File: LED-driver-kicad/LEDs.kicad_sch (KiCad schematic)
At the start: 54 parts, among them Q8 Q_NMOS_GDS, U6 MIC3205YML-TR, U7 MIC3205YML-TR, U8 MIC3205YML-TR

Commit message: initial PCB layout
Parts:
- removed D10: BAT42, Diode_THT:D_DO-35_SOD27_P7.62mm_Horizontal, symbol Diode:BAT42
- added D10: SD103AWS, Diode_SMD:D_SOD-323_HandSoldering, symbol Device:D_Schottky_Small
- D17, D24: value BAT42 -> SD103AWS; footprint Diode_THT:D_DO-35_SOD27_P7.62mm_Horizontal -> Diode_SMD:D_SOD-323_HandSoldering; symbol Diode:BAT42 -> Device:D_Schottky_Small
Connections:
- net +28V: now also D10.1 (K)
- net at L4.2, Q8.2 (D): now also D10.2 (A)
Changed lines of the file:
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@@
     (stroke (width 0) (type default))
   )
-  (wire (pts (xy 174.625 63.5) (xy 202.565 63.5))
+  (wire (pts (xy 174.625 63.5) (xy 203.835 63.5))
     (stroke (width 0) (type default))
   )
@@
     (stroke (width 0) (type default))
   )
-  (wire (pts (xy 83.185 114.3) (xy 117.475 114.3))
+  (wire (pts (xy 81.915 114.3) (xy 117.475 114.3))
     (stroke (width 0) (type default))
   )
@@
     (stroke (width 0) (type default))
   )
-  (wire (pts (xy 47.625 31.75) (xy 75.565 31.75))
+  (wire (pts (xy 47.625 31.75) (xy 76.2 31.75))
     (stroke (width 0) (type default))
   )
@@
     (stroke (width 0) (type default))
   )
-  (wire (pts (xy 47.625 114.3) (xy 75.565 114.3))
-    (stroke (width 0) (type default))
-  )
   (wire (pts (xy 186.69 82.55) (xy 186.69 93.98))
     (stroke (width 0) (type default))
@@
     (stroke (width 0) (type default))
   )
-  (wire (pts (xy 210.185 63.5) (xy 244.475 63.5))
+  (wire (pts (xy 208.915 63.5) (xy 244.475 63.5))
     (stroke (width 0) (type default))
   )
@@
     (stroke (width 0) (type default))
   )
-  (wire (pts (xy 83.185 31.75) (xy 117.475 31.75))
-    (stroke (width 0) (type default))
-  )
   (wire (pts (xy 80.645 133.35) (xy 102.235 133.35))
     (stroke (width 0) (type default))
   )
+  (wire (pts (xy 81.28 31.75) (xy 117.475 31.75))
+    (stroke (width 0) (type default))
+  )
   (wire (pts (xy 76.835 167.64) (xy 76.835 169.545))
     (stroke (width 0) (type default))
@@
   )
   (wire (pts (xy 186.69 73.025) (xy 186.69 82.55))
+    (stroke (width 0) (type default))
+  )
+  (wire (pts (xy 47.625 114.3) (xy 76.835 114.3))
     (stroke (width 0) (type default))
   )
@@
     )
   )
-  (symbol (lib_id "Diode:BAT42") (at 206.375 63.5 0) (unit 1)
+  (symbol (lib_id "Device:D_Schottky_Small") (at 206.375 63.5 0) (unit 1)
     (in_bom yes) (on_board yes) (dnp no)
     (property "Reference" "D17" (at 206.375 58.42 0)
       (effects (font (size 1.27 1.27)))
     )
-    (property "Value" "BAT42" (at 206.375 60.96 0)
-      (effects (font (size 1.27 1.27)))
-    )
-    (property "Footprint" "Diode_THT:D_DO-35_SOD27_P7.62mm_Horizontal" (at 206.375 67.945 0)
-      (effects (font (size 1.27 1.27)) hide)
-    )
-    (property "Datasheet" "http://www.vishay.com/docs/85660/bat42.pdf" (at 206.375 63.5 0)
+    (property "Value" "SD103AWS" (at 206.375 60.96 0)
+      (effects (font (size 1.27 1.27)))
+    )
+    (property "Footprint" "Diode_SMD:D_SOD-323_HandSoldering" (at 206.375 63.5 90)
+      (effects (font (size 1.27 1.27)) hide)
+    )
+    (property "Datasheet" "~" (at 206.375 63.5 90)
       (effects (font (size 1.27 1.27)) hide)
     )
@@
     )
   )
+  (symbol (lib_id "Device:D_Schottky_Small") (at 78.74 31.75 0) (unit 1)
+    (in_bom yes) (on_board yes) (dnp no)
+    (property "Reference" "D10" (at 78.74 26.67 0)
+      (effects (font (size 1.27 1.27)))
+    )
+    (property "Value" "SD103AWS" (at 78.74 29.21 0)
+      (effects (font (size 1.27 1.27)))
+    )
+    (property "Footprint" "Diode_SMD:D_SOD-323_HandSoldering" (at 78.74 31.75 90)
+      (effects (font (size 1.27 1.27)) hide)
+    )
+    (property "Datasheet" "~" (at 78.74 31.75 90)
+      (effects (font (size 1.27 1.27)) hide)
+    )
+    (pin "1")
+    (pin "2")
+    (instances
+      (project "LED-driver-kicad"
+        (path "/2b071084-2ab6-4896-84cc-45b211479417/250319e1-deb8-4d57-8ee9-fb5c0c792a75"
+          (reference "D10") (unit 1)
+        )
+      )
+    )
+  )
   (symbol (lib_id "power:GND") (at 89.535 171.45 0) (unit 1)
     (in_bom yes) (on_board yes) (dnp no)
@@
         (path "/2b071084-2ab6-4896-84cc-45b211479417/b9376bb1-65c2-486f-9413-68de3cd30605"
           (reference "#PWR058") (unit 1)
-        )
-      )
-    )
-  )
-  (symbol (lib_id "Diode:BAT42") (at 79.375 31.75 0) (unit 1)
-    (in_bom yes) (on_board yes) (dnp no)
-    (property "Reference" "D10" (at 79.375 26.67 0)
-      (effects (font (size 1.27 1.27)))
-    )
-    (property "Value" "BAT42" (at 79.375 29.21 0)
-      (effects (font (size 1.27 1.27)))
-    )
-    (property "Footprint" "Diode_THT:D_DO-35_SOD27_P7.62mm_Horizontal" (at 79.375 36.195 0)
-      (effects (font (size 1.27 1.27)) hide)
-    )
-    (property "Datasheet" "http://www.vishay.com/docs/85660/bat42.pdf" (at 79.375 31.75 0)
-      (effects (font (size 1.27 1.27)) hide)
-    )
-    (pin "1")
-    (pin "2")
-    (instances
-      (project "LED-driver-kicad"
-        (path "/2b071084-2ab6-4896-84cc-45b211479417/250319e1-deb8-4d57-8ee9-fb5c0c792a75"
-          (reference "D10") (unit 1)
-        )
-        (path "/2b071084-2ab6-4896-84cc-45b211479417/b9376bb1-65c2-486f-9413-68de3cd30605"
-          (reference "D37") (unit 1)
         )
       )
@@
     )
   )
-  (symbol (lib_id "Diode:BAT42") (at 79.375 114.3 0) (unit 1)
+  (symbol (lib_id "Device:D_Schottky_Small") (at 79.375 114.3 0) (unit 1)
     (in_bom yes) (on_board yes) (dnp no)
     (property "Reference" "D24" (at 79.375 109.22 0)
       (effects (font (size 1.27 1.27)))
     )
-    (property "Value" "BAT42" (at 79.375 111.76 0)
-      (effects (font (size 1.27 1.27)))
-    )
-    (property "Footprint" "Diode_THT:D_DO-35_SOD27_P7.62mm_Horizontal" (at 79.375 118.745 0)
-      (effects (font (size 1.27 1.27)) hide)
-    )
-    (property "Datasheet" "http://www.vishay.com/docs/85660/bat42.pdf" (at 79.375 114.3 0)
-      (effects (font (size 1.27 1.27)) hide)
-    )
+    (property "Value" "SD103AWS" (at 79.375 111.76 0)
+      (effects (font (size 1.27 1.27)))
+    )
+    (property "Footprint" "Diode_SMD:D_SOD-323_HandSoldering" (at 79.375 114.3 90)
+      (effects (font (size 1.27 1.27)) hide)
+    )
+    (property "Datasheet" "~" (at 79.375 114.3 90)
+      (effects (font (size 1.27 1.27)) hide)
+    )

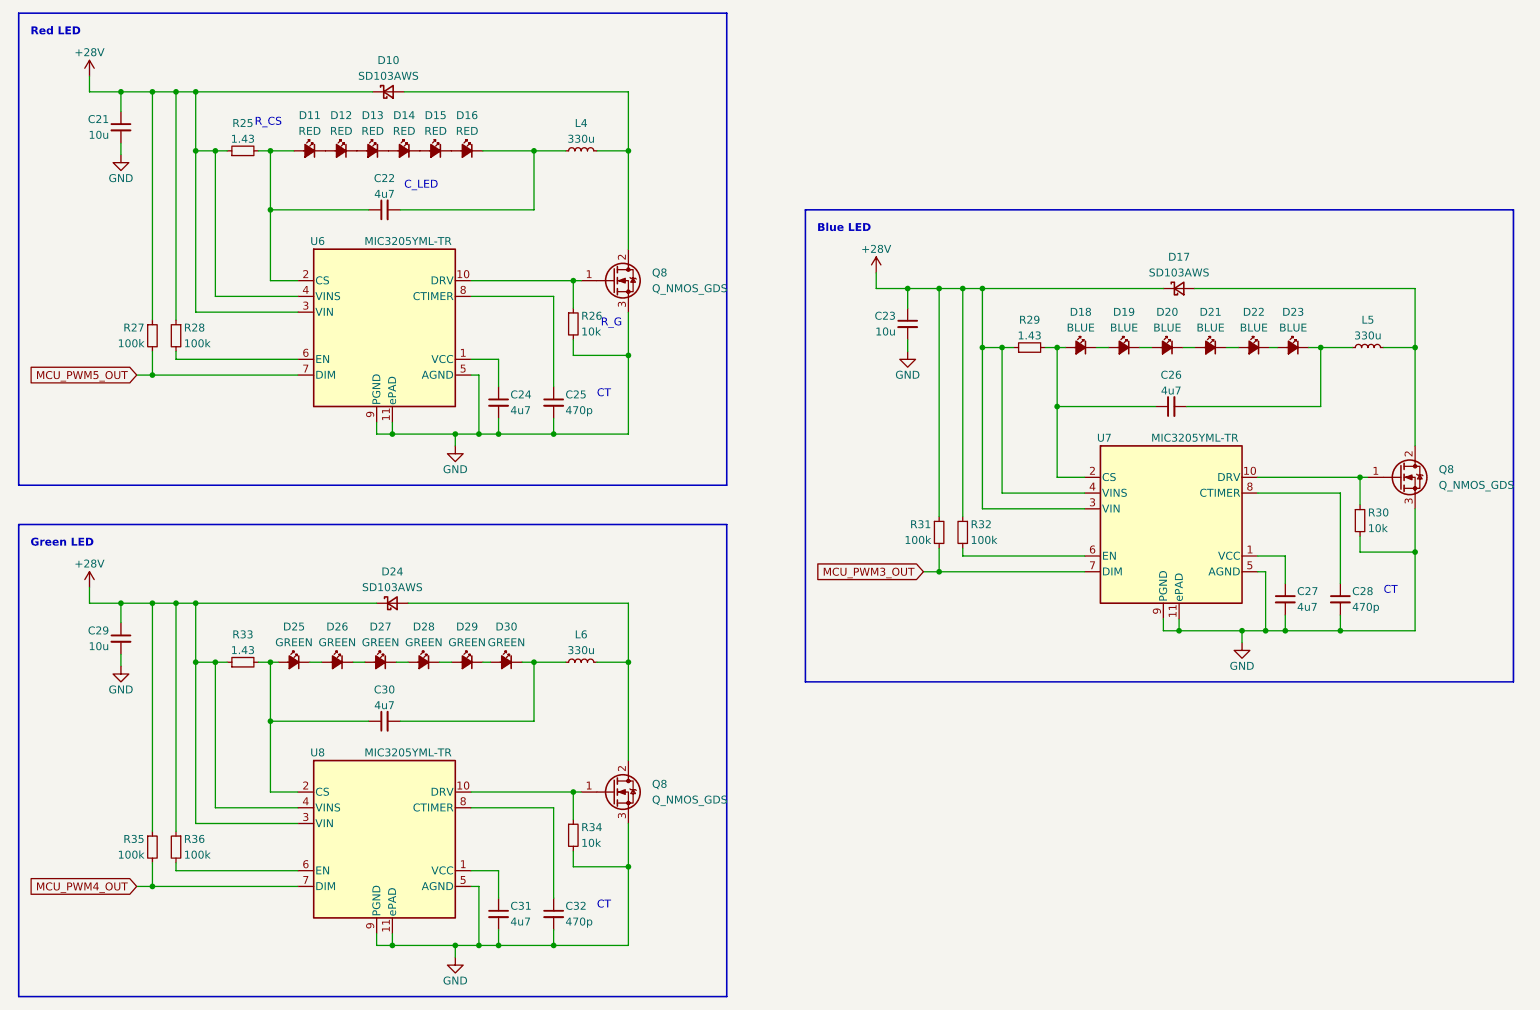
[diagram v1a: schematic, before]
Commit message: add test points, net ties to schematics
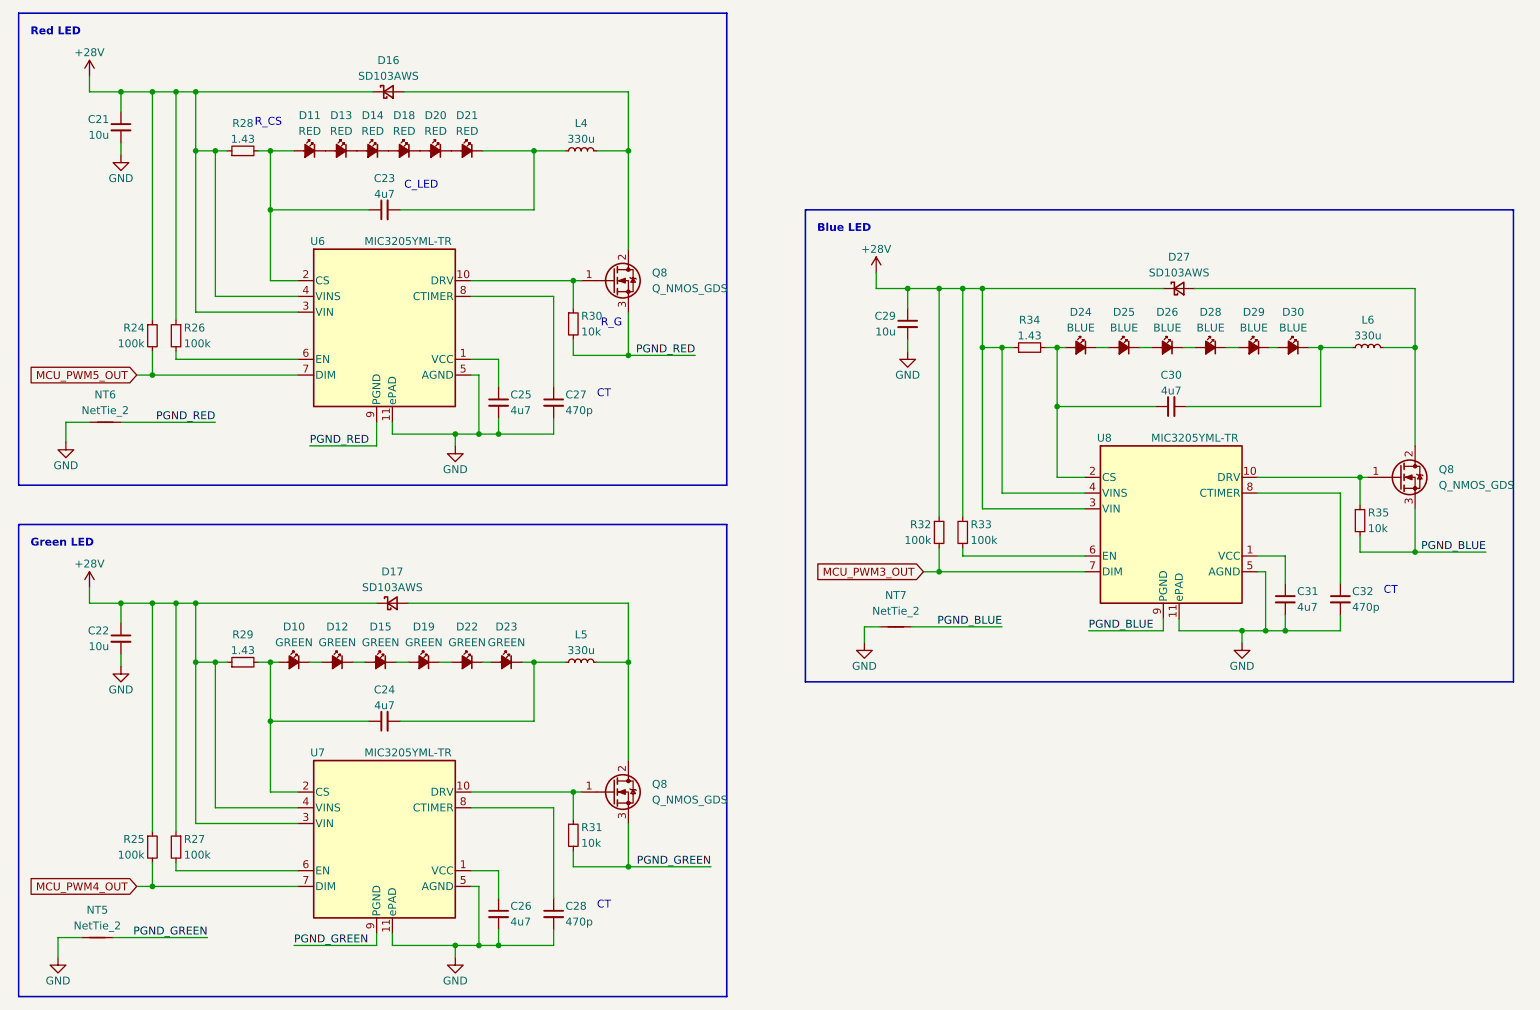
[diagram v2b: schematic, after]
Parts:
- added NT5, NT6, NT7: NetTie_2, NetTie:NetTie-2_SMD_Pad0.5mm, symbol Device:NetTie_2
- renumbered C29 to C22, C22 to C23, C30 to C24, C24 to C25, C31 to C26, C25 to C27, C32 to C28, C23 to C29, C26 to C30, C27 to C31, C28 to C32, D25 to D10, D26 to D12, D12 to D13, D13 to D14, D27 to D15, D10 to D16, D24 to D17, D14 to D18, D28 to D19, D15 to D20, D16 to D21, D29 to D22, D30 to D23, D18 to D24, D19 to D25, D20 to D26, D17 to D27, D21 to D28, D22 to D29, D23 to D30, L6 to L5, L5 to L6, R27 to R24, R35 to R25, R28 to R26, R36 to R27, R25 to R28, R33 to R29, R26 to R30, R34 to R31, R31 to R32, R32 to R33, R29 to R34, R30 to R35, U8 to U7, U7 to U8
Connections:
- net GND: now also NT5.1, NT6.1, NT7.1; no longer Q8.3 (S), Q8.3 (S), Q8.3 (S), R30.2, R31.2, R35.2, U6.9 (PGND), U7.9 (PGND), U8.9 (PGND)
- new net PGND_BLUE: NT7.2, Q8.3 (S), R35.2, U8.9 (PGND)
- new net PGND_GREEN: NT5.2, Q8.3 (S), R31.2, U7.9 (PGND)
- new net PGND_RED: NT6.2, Q8.3 (S), R30.2, U6.9 (PGND)
